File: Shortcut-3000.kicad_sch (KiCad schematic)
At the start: 47 parts, among them J1 MagneticPogo_1x05_Female, J10 MagneticPogo_1x05_Female, J11 MagneticPogo_1x05_Female, J12 MagneticPogo_1x05_Female, J2 MagneticPogo_1x05_Female, J3 MagneticPogo_1x05_Female, J4 MagneticPogo_1x05_Female, J5 MagneticPogo_1x05_Female, J6 MagneticPogo_1x05_Female, J7 MagneticPogo_1x05_Female, J8 MagneticPogo_1x05_Female, J9 MagneticPogo_1x05_Female, SW1 SW_Push, SW10 SW_Push, SW11 SW_Push, SW12 SW_Push, SW13 SW_Push, SW14 SW_Push, SW15 SW_Push, SW16 RotaryEncoder_Switch, SW17 RotaryEncoder_Switch, SW2 SW_Push, SW3 SW_Push, SW4 SW_Push, SW5 SW_Push, SW6 SW_Push, SW7 SW_Push, SW8 SW_Push, SW9 SW_Push

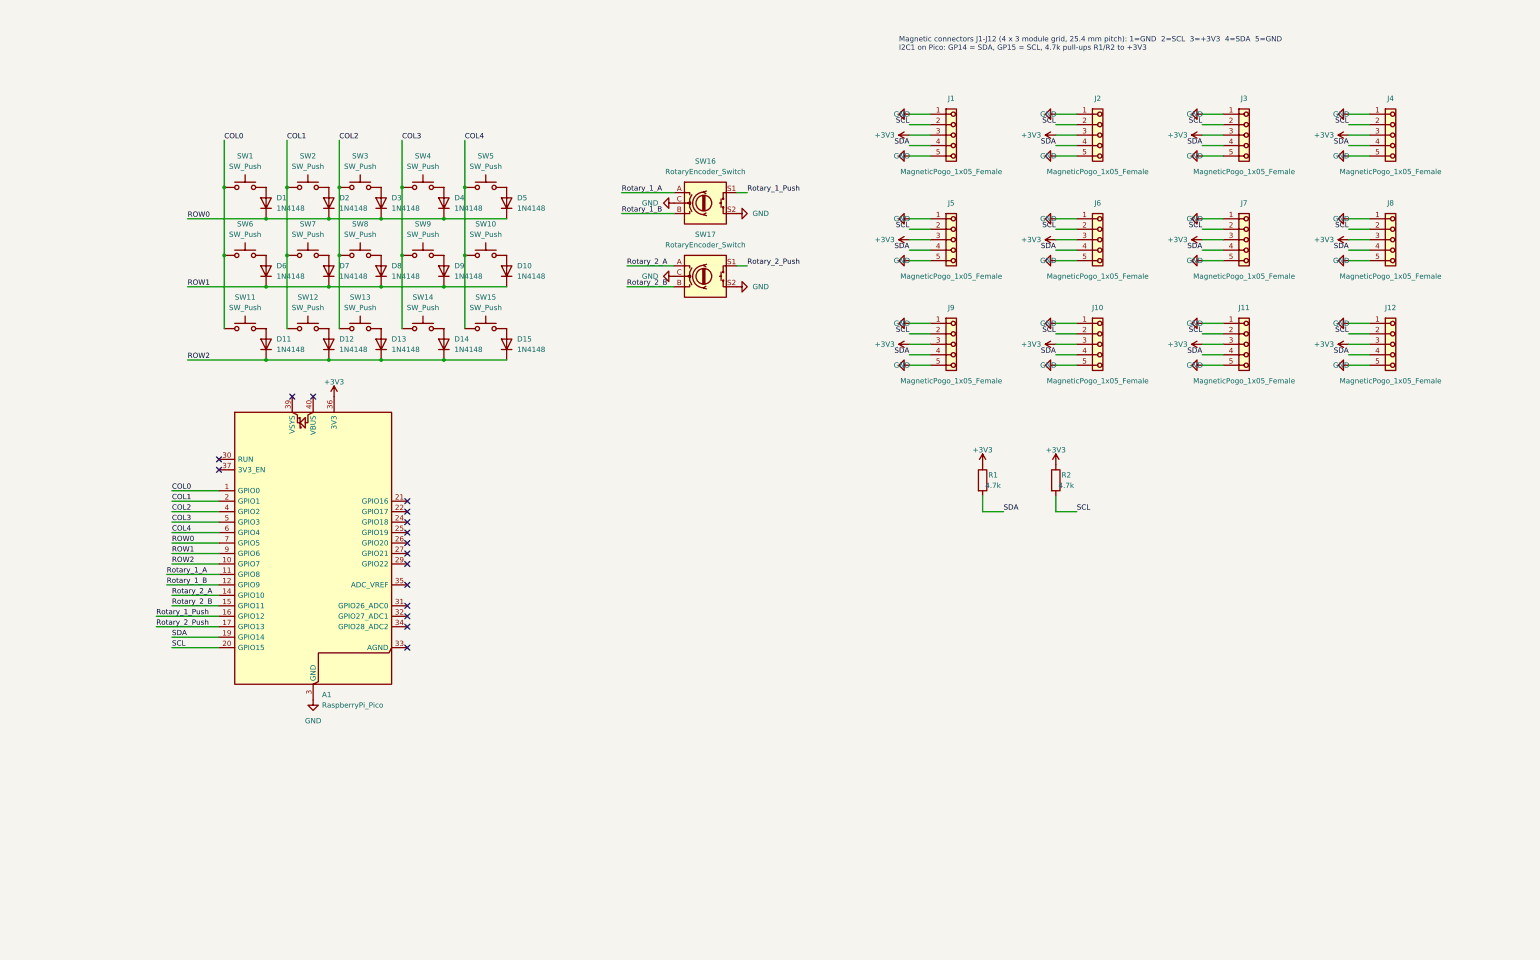
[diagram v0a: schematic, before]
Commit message: Switch to RP2040-Zero and route connectors through TCA9548A muxes
- Add Waveshare RP2040-Zero symbol and castellated footprint to the
  project library (dimensions from Waveshare's drawing) and replace the
  Raspberry Pi Pico with it
- Split the connectors across both I2C buses: J1-J6 on I2C0 (GP4/GP5),
  J7-J12 on I2C1 (GP6/GP7)
- Repurpose connector pin 5 as an open-drain INT line, shared per bus
  (INT0 = GP8, INT1 = GP9)
- Give each connector its own TCA9548A channel: J1-J6 on U1 ch 0-5,
  J7-J12 on U2 ch 0-5; channels 6-7 marked no-connect
- Ground mux pin 12, add 10k RESET pull-ups (R7-R8), 4.7k upstream
  pull-ups (R1-R4), 10k INT pull-ups (R5-R6) and 4.7k per-channel
  pull-ups (R9-R32)

Co-Authored-By: Claude Opus 5.5 <noreply@anthropic.com>
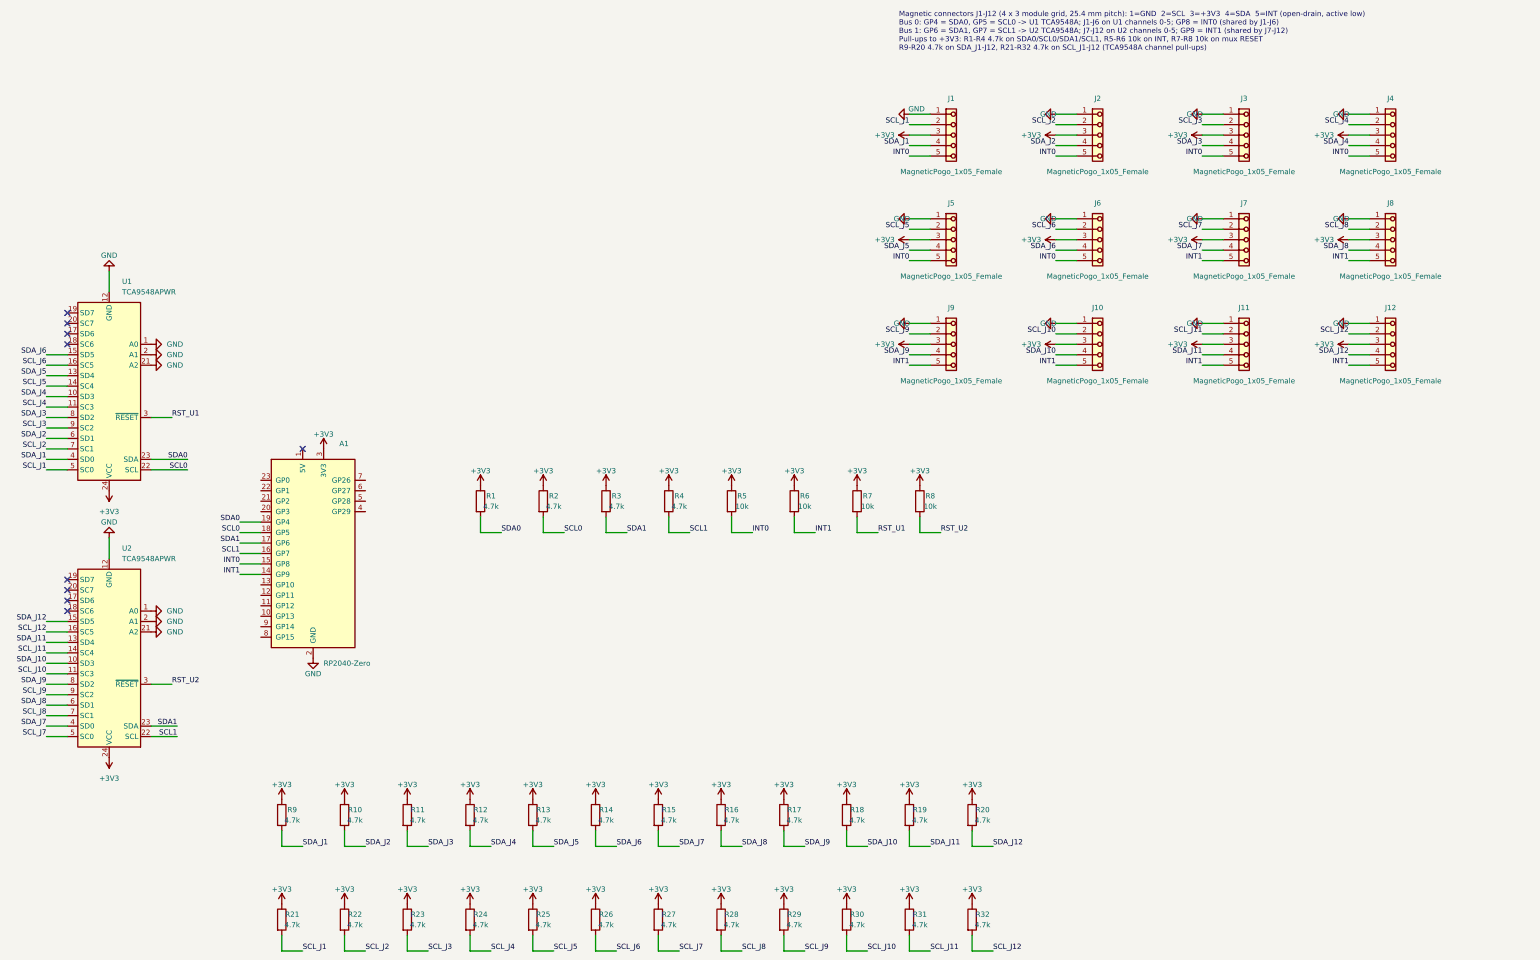
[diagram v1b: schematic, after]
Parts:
- removed A1: RaspberryPi_Pico, Module:RaspberryPi_Pico_Common_THT, symbol MCU_Module:RaspberryPi_Pico
- removed D1, D10, D11, D12, D13, D14, D15, D2, D3, D4, D5, D6, D7, D8, D9: 1N4148, Diode_THT:D_DO-35_SOD27_P7.62mm_Horizontal, symbol Diode:1N4148
- removed SW1, SW10, SW11, SW12, SW13, SW14, SW15, SW2, SW3, SW4, SW5, SW6, SW7, SW8, SW9: SW_Push, PCM_marbastlib-mx:SW_MX_HS_CPG151101S11_1u, symbol Switch:SW_Push
- removed SW16, SW17: RotaryEncoder_Switch, Rotary_Encoder:RotaryEncoder_Alps_EC11E-Switch_Vertical_H20mm, symbol Device:RotaryEncoder_Switch
- added A1: RP2040-Zero, Shortcut-3000:RP2040-Zero_Castellated, symbol Shortcut-3000:RP2040-Zero
- added R10, R11, R12, R13, R14, R15, R16, R17, R18, R19, R20, R21, R22, R23, R24, R25, R26, R27, R28, R29, R3, R30, R31, R32, R4, R9: 4.7k, Resistor_THT:R_Axial_DIN0207_L6.3mm_D2.5mm_P7.62mm_Horizontal, symbol Device:R
- added R5, R6, R7, R8: 10k, Resistor_THT:R_Axial_DIN0207_L6.3mm_D2.5mm_P7.62mm_Horizontal, symbol Device:R
- added U1, U2: TCA9548APWR, Package_SO:TSSOP-24_4.4x7.8mm_P0.65mm, symbol Interface_Expansion:TCA9548APWR
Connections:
- net +3V3: now also A1.3 (3V3), R10.1, R11.1, R12.1, R13.1, R14.1, R15.1, R16.1, R17.1, R18.1, R19.1, R20.1, R21.1, R22.1, R23.1, R24.1, R25.1, R26.1, R27.1, R28.1, R29.1, R3.1, R30.1, R31.1, R32.1, R4.1, R5.1, R6.1, R7.1, R8.1, R9.1, U1.24 (VCC), U2.24 (VCC)
- net GND: now also A1.2 (GND), U1.1 (A0), U1.12 (GND), U1.2 (A1), U1.21 (A2), U2.1 (A0), U2.12 (GND), U2.2 (A1), U2.21 (A2); no longer J1.5 (Pin_5), J10.5 (Pin_5), J11.5 (Pin_5), J12.5 (Pin_5), J2.5 (Pin_5), J3.5 (Pin_5), J4.5 (Pin_5), J5.5 (Pin_5), J6.5 (Pin_5), J7.5 (Pin_5), J8.5 (Pin_5), J9.5 (Pin_5)
- removed net SCL: J1.2 (Pin_2), J10.2 (Pin_2), J11.2 (Pin_2), J12.2 (Pin_2), J2.2 (Pin_2), J3.2 (Pin_2), J4.2 (Pin_2), J5.2 (Pin_2), J6.2 (Pin_2), J7.2 (Pin_2), J8.2 (Pin_2), J9.2 (Pin_2), R2.2
- removed net SDA: J1.4 (Pin_4), J10.4 (Pin_4), J11.4 (Pin_4), J12.4 (Pin_4), J2.4 (Pin_4), J3.4 (Pin_4), J4.4 (Pin_4), J5.4 (Pin_4), J6.4 (Pin_4), J7.4 (Pin_4), J8.4 (Pin_4), J9.4 (Pin_4), R1.2
- new net INT0: A1.15 (GP8), J1.5 (Pin_5), J2.5 (Pin_5), J3.5 (Pin_5), J4.5 (Pin_5), J5.5 (Pin_5), J6.5 (Pin_5), R5.2
- new net INT1: A1.14 (GP9), J10.5 (Pin_5), J11.5 (Pin_5), J12.5 (Pin_5), J7.5 (Pin_5), J8.5 (Pin_5), J9.5 (Pin_5), R6.2
- new net RST_U1: R7.2, U1.3 (~{RESET})
- new net RST_U2: R8.2, U2.3 (~{RESET})
- new net SCL0: A1.18 (GP5), R2.2, U1.22 (SCL)
- new net SCL1: A1.16 (GP7), R4.2, U2.22 (SCL)
- new net SCL_J1: J1.2 (Pin_2), R21.2, U1.5 (SC0)
- new net SCL_J10: J10.2 (Pin_2), R30.2, U2.11 (SC3)
- new net SCL_J11: J11.2 (Pin_2), R31.2, U2.14 (SC4)
- new net SCL_J12: J12.2 (Pin_2), R32.2, U2.16 (SC5)
- new net SCL_J2: J2.2 (Pin_2), R22.2, U1.7 (SC1)
- new net SCL_J3: J3.2 (Pin_2), R23.2, U1.9 (SC2)
- new net SCL_J4: J4.2 (Pin_2), R24.2, U1.11 (SC3)
- new net SCL_J5: J5.2 (Pin_2), R25.2, U1.14 (SC4)
- new net SCL_J6: J6.2 (Pin_2), R26.2, U1.16 (SC5)
- new net SCL_J7: J7.2 (Pin_2), R27.2, U2.5 (SC0)
- new net SCL_J8: J8.2 (Pin_2), R28.2, U2.7 (SC1)
- new net SCL_J9: J9.2 (Pin_2), R29.2, U2.9 (SC2)
- new net SDA0: A1.19 (GP4), R1.2, U1.23 (SDA)
- new net SDA1: A1.17 (GP6), R3.2, U2.23 (SDA)
- new net SDA_J1: J1.4 (Pin_4), R9.2, U1.4 (SD0)
- new net SDA_J10: J10.4 (Pin_4), R18.2, U2.10 (SD3)
- new net SDA_J11: J11.4 (Pin_4), R19.2, U2.13 (SD4)
- new net SDA_J12: J12.4 (Pin_4), R20.2, U2.15 (SD5)
- new net SDA_J2: J2.4 (Pin_4), R10.2, U1.6 (SD1)
- new net SDA_J3: J3.4 (Pin_4), R11.2, U1.8 (SD2)
- new net SDA_J4: J4.4 (Pin_4), R12.2, U1.10 (SD3)
- new net SDA_J5: J5.4 (Pin_4), R13.2, U1.13 (SD4)
- new net SDA_J6: J6.4 (Pin_4), R14.2, U1.15 (SD5)
- new net SDA_J7: J7.4 (Pin_4), R15.2, U2.4 (SD0)
- new net SDA_J8: J8.4 (Pin_4), R16.2, U2.6 (SD1)
- new net SDA_J9: J9.4 (Pin_4), R17.2, U2.8 (SD2)
- no-connect marks 16 -> 9
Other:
- note added: "Magnetic connectors J1-J12 (4 x 3 module grid, 25.4 mm pitch): 1=GND 2=SCL 3=+3V3 4=SDA 5=INT (open-drain, active low) Bus 0: GP4 = SDA0, GP5 = SCL0 -> U1 TCA9548A; J1-J6 on U1 channels 0-5; GP8 = INT0 (shared by J1-J6) Bus 1: GP6 = SDA1, GP7 = SCL1 -> U2 TCA9548A; J7-J12 on U2 channels 0-5; GP9 = INT1 (shared by J7-J12) Pull-ups to +3V3: R1-R4 4.7k on SDA0/SCL0/SDA1/SCL1, R5-R6 10k on INT, R7-R8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"
- note removed: "Magnetic connectors J1-J12 (4 x 3 module grid, 25.4 mm pitch): 1=GND 2=SCL 3=+3V3 4=SDA 5=GND I2C1 on Pico: GP14 = SDA, GP15 = SCL, 4.7k pull-ups R1/R2 to +3V3"

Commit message: Backup before removing PCB routing
Co-Authored-By: Claude Opus 5.5 <noreply@anthropic.com>
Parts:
- R1, R10, R11, R12, R13, R14, R15, R16, R17, R18, R19, R2, R20, R21, R22, R23, R24, R25, R26, R27, R28, R29, R3, R30, R31, R32, R4, R5, R6, R7, R8, R9: footprint Resistor_THT:R_Axial_DIN0207_L6.3mm_D2.5mm_P7.62mm_Horizontal -> Resistor_SMD:R_0805_2012Metric
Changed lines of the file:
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@@
 			)
 		)
-		(property "Footprint" "Resistor_THT:R_Axial_DIN0207_L6.3mm_D2.5mm_P7.62mm_Horizontal"
+		(property "Footprint" "Resistor_SMD:R_0805_2012Metric"
 			(at 132.08 215.9 0)
 			(hide yes)
@@
 			)
 		)
-		(property "Footprint" "Resistor_THT:R_Axial_DIN0207_L6.3mm_D2.5mm_P7.62mm_Horizontal"
+		(property "Footprint" "Resistor_SMD:R_0805_2012Metric"
 			(at 147.32 241.3 0)
 			(hide yes)
@@
 			)
 		)
-		(property "Footprint" "Resistor_THT:R_Axial_DIN0207_L6.3mm_D2.5mm_P7.62mm_Horizontal"
+		(property "Footprint" "Resistor_SMD:R_0805_2012Metric"
 			(at 116.84 241.3 0)
 			(hide yes)
@@
 			)
 		)
-		(property "Footprint" "Resistor_THT:R_Axial_DIN0207_L6.3mm_D2.5mm_P7.62mm_Horizontal"
+		(property "Footprint" "Resistor_SMD:R_0805_2012Metric"
 			(at 165.1 139.7 0)
 			(hide yes)
@@
 			)
 		)
-		(property "Footprint" "Resistor_THT:R_Axial_DIN0207_L6.3mm_D2.5mm_P7.62mm_Horizontal"
+		(property "Footprint" "Resistor_SMD:R_0805_2012Metric"
 			(at 238.76 241.3 0)
 			(hide yes)
@@
 			)
 		)
-		(property "Footprint" "Resistor_THT:R_Axial_DIN0207_L6.3mm_D2.5mm_P7.62mm_Horizontal"
+		(property "Footprint" "Resistor_SMD:R_0805_2012Metric"
 			(at 241.3 139.7 0)
 			(hide yes)
@@
 			)
 		)
-		(property "Footprint" "Resistor_THT:R_Axial_DIN0207_L6.3mm_D2.5mm_P7.62mm_Horizontal"
+		(property "Footprint" "Resistor_SMD:R_0805_2012Metric"
 			(at 271.78 139.7 0)
 			(hide yes)
@@
 			)
 		)
-		(property "Footprint" "Resistor_THT:R_Axial_DIN0207_L6.3mm_D2.5mm_P7.62mm_Horizontal"
+		(property "Footprint" "Resistor_SMD:R_0805_2012Metric"
 			(at 284.48 215.9 0)
 			(hide yes)
@@
 			)
 		)
-		(property "Footprint" "Resistor_THT:R_Axial_DIN0207_L6.3mm_D2.5mm_P7.62mm_Horizontal"
+		(property "Footprint" "Resistor_SMD:R_0805_2012Metric"
 			(at 210.82 139.7 0)
 			(hide yes)
@@
 			)
 		)
-		(property "Footprint" "Resistor_THT:R_Axial_DIN0207_L6.3mm_D2.5mm_P7.62mm_Horizontal"
+		(property "Footprint" "Resistor_SMD:R_0805_2012Metric"
 			(at 177.8 215.9 0)
 			(hide yes)
@@
 			)
 		)
-		(property "Footprint" "Resistor_THT:R_Axial_DIN0207_L6.3mm_D2.5mm_P7.62mm_Horizontal"
+		(property "Footprint" "Resistor_SMD:R_0805_2012Metric"
 			(at 269.24 241.3 0)
 			(hide yes)
@@
 			)
 		)
-		(property "Footprint" "Resistor_THT:R_Axial_DIN0207_L6.3mm_D2.5mm_P7.62mm_Horizontal"
+		(property "Footprint" "Resistor_SMD:R_0805_2012Metric"
 			(at 254 215.9 0)
 			(hide yes)
@@
 			)
 		)
-		(property "Footprint" "Resistor_THT:R_Axial_DIN0207_L6.3mm_D2.5mm_P7.62mm_Horizontal"
+		(property "Footprint" "Resistor_SMD:R_0805_2012Metric"
 			(at 193.04 215.9 0)
 			(hide yes)
@@
 			)
 		)
-		(property "Footprint" "Resistor_THT:R_Axial_DIN0207_L6.3mm_D2.5mm_P7.62mm_Horizontal"
+		(property "Footprint" "Resistor_SMD:R_0805_2012Metric"
 			(at 193.04 241.3 0)
 			(hide yes)
@@
 			)
 		)
-		(property "Footprint" "Resistor_THT:R_Axial_DIN0207_L6.3mm_D2.5mm_P7.62mm_Horizontal"
+		(property "Footprint" "Resistor_SMD:R_0805_2012Metric"
 			(at 208.28 215.9 0)
 			(hide yes)
@@
 			)
 		)
-		(property "Footprint" "Resistor_THT:R_Axial_DIN0207_L6.3mm_D2.5mm_P7.62mm_Horizontal"
+		(property "Footprint" "Resistor_SMD:R_0805_2012Metric"
 			(at 180.34 139.7 0)
 			(hide yes)
@@
 			)
 		)
-		(property "Footprint" "Resistor_THT:R_Axial_DIN0207_L6.3mm_D2.5mm_P7.62mm_Horizontal"
+		(property "Footprint" "Resistor_SMD:R_0805_2012Metric"
 			(at 284.48 241.3 0)
 			(hide yes)
@@
 			)
 		)
-		(property "Footprint" "Resistor_THT:R_Axial_DIN0207_L6.3mm_D2.5mm_P7.62mm_Horizontal"
+		(property "Footprint" "Resistor_SMD:R_0805_2012Metric"
 			(at 195.58 139.7 0)
 			(hide yes)
@@
 			)
 		)
-		(property "Footprint" "Resistor_THT:R_Axial_DIN0207_L6.3mm_D2.5mm_P7.62mm_Horizontal"
+		(property "Footprint" "Resistor_SMD:R_0805_2012Metric"
 			(at 223.52 241.3 0)
 			(hide yes)
@@
 			)
 		)
-		(property "Footprint" "Resistor_THT:R_Axial_DIN0207_L6.3mm_D2.5mm_P7.62mm_Horizontal"
+		(property "Footprint" "Resistor_SMD:R_0805_2012Metric"
 			(at 116.84 215.9 0)
 			(hide yes)
@@
 			)
 		)
-		(property "Footprint" "Resistor_THT:R_Axial_DIN0207_L6.3mm_D2.5mm_P7.62mm_Horizontal"
+		(property "Footprint" "Resistor_SMD:R_0805_2012Metric"
 			(at 223.52 215.9 0)
 			(hide yes)
@@
 			)
 		)
-		(property "Footprint" "Resistor_THT:R_Axial_DIN0207_L6.3mm_D2.5mm_P7.62mm_Horizontal"
+		(property "Footprint" "Resistor_SMD:R_0805_2012Metric"
 			(at 256.54 139.7 0)
 			(hide yes)
@@
 			)
 		)
-		(property "Footprint" "Resistor_THT:R_Axial_DIN0207_L6.3mm_D2.5mm_P7.62mm_Horizontal"
+		(property "Footprint" "Resistor_SMD:R_0805_2012Metric"
 			(at 132.08 241.3 0)
 			(hide yes)
@@
 			)
 		)
-		(property "Footprint" "Resistor_THT:R_Axial_DIN0207_L6.3mm_D2.5mm_P7.62mm_Horizontal"
+		(property "Footprint" "Resistor_SMD:R_0805_2012Metric"
 			(at 269.24 215.9 0)
 			(hide yes)
@@
 			)
 		)
-		(property "Footprint" "Resistor_THT:R_Axial_DIN0207_L6.3mm_D2.5mm_P7.62mm_Horizontal"
+		(property "Footprint" "Resistor_SMD:R_0805_2012Metric"
 			(at 177.8 241.3 0)
 			(hide yes)
@@
 			)
 		)
-		(property "Footprint" "Resistor_THT:R_Axial_DIN0207_L6.3mm_D2.5mm_P7.62mm_Horizontal"
+		(property "Footprint" "Resistor_SMD:R_0805_2012Metric"
 			(at 226.06 139.7 0)
 			(hide yes)
@@
 			)
 		)
-		(property "Footprint" "Resistor_THT:R_Axial_DIN0207_L6.3mm_D2.5mm_P7.62mm_Horizontal"
+		(property "Footprint" "Resistor_SMD:R_0805_2012Metric"
 			(at 208.28 241.3 0)
 			(hide yes)
@@
 			)
 		)
-		(property "Footprint" "Resistor_THT:R_Axial_DIN0207_L6.3mm_D2.5mm_P7.62mm_Horizontal"
+		(property "Footprint" "Resistor_SMD:R_0805_2012Metric"
 			(at 162.56 215.9 0)
 			(hide yes)
@@
 			)
 		)
-		(property "Footprint" "Resistor_THT:R_Axial_DIN0207_L6.3mm_D2.5mm_P7.62mm_Horizontal"
+		(property "Footprint" "Resistor_SMD:R_0805_2012Metric"
 			(at 238.76 215.9 0)
 			(hide yes)
@@
 			)
 		)
-		(property "Footprint" "Resistor_THT:R_Axial_DIN0207_L6.3mm_D2.5mm_P7.62mm_Horizontal"
+		(property "Footprint" "Resistor_SMD:R_0805_2012Metric"
 			(at 162.56 241.3 0)
 			(hide yes)
@@
 			)
 		)
-		(property "Footprint" "Resistor_THT:R_Axial_DIN0207_L6.3mm_D2.5mm_P7.62mm_Horizontal"
+		(property "Footprint" "Resistor_SMD:R_0805_2012Metric"
 			(at 254 241.3 0)
 			(hide yes)
@@
 			)
 		)
-		(property "Footprint" "Resistor_THT:R_Axial_DIN0207_L6.3mm_D2.5mm_P7.62mm_Horizontal"
+		(property "Footprint" "Resistor_SMD:R_0805_2012Metric"
 			(at 147.32 215.9 0)
 			(hide yes)

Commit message: Change pogo pin hole size and add 4-pin magnetic pogo footprints
Co-Authored-By: Claude Opus 5.5 <noreply@anthropic.com>
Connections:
- net +5V: now reaches A1.1 (5V)
- no-connect marks 9 -> 8
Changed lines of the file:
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@@
 	)
 	(no_connect
-		(at 121.92 127)
-	)
-	(no_connect
 		(at 64.77 163.83)
 	)
@@
 					(unit 1)
 				)
+			)
+		)
+	)
+	(symbol
+		(lib_id "power:+5V")
+		(at 121.92 127 0)
+		(unit 1)
+		(body_style 1)
+		(exclude_from_sim no)
+		(in_bom yes)
+		(on_board yes)
+		(in_pos_files yes)
+		(dnp no)
+		(fields_autoplaced yes)
+		(property "Reference" "#PWR032"
+			(at 121.92 130.81 0)
+			(hide yes)
+			(show_name no)
+			(do_not_autoplace no)
+			(effects
+				(font
+					(size 1.27 1.27)
+				)
+			)
+		)
+		(property "Value" "+5V"
+			(at 121.92 121.92 0)
+			(show_name no)
+			(do_not_autoplace no)
+			(effects
+				(font
+					(size 1.27 1.27)
+				)
+			)
+		)
+		(property "Footprint" ""
+			(at 121.92 127 0)
+			(hide yes)
+			(show_name no)
+			(do_not_autoplace no)
+			(effects
+				(font
+					(size 1.27 1.27)
+				)
+			)
+		)
+		(property "Datasheet" ""
+			(at 121.92 127 0)
+			(hide yes)
+			(show_name no)
+			(do_not_autoplace no)
+			(effects
+				(font
+					(size 1.27 1.27)
+				)
+			)
+		)
+		(property "Description" "Power symbol creates a global label with name \"+5V\""
+			(at 121.92 127 0)
+			(hide yes)
+			(show_name no)
+			(do_not_autoplace no)
+			(effects
+				(font
+					(size 1.27 1.27)
+				)
+			)
+		)
+		(pin "1"
+		)
+		(instances
+			(project "Shortcut-3000"
+				(path "/6a8f3e6a-bfaa-48b7-95b3-152f71a0a93a"
+					(reference "#PWR032")
+					(unit 1)
+				)
